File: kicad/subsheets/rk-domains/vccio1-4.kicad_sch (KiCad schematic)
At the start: 6 parts, among them U5 RK3566

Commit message: Mark as R1.0
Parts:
- renumbered C134 to C113, C129 to C114, C135 to C115, C137 to C116, R47 to R44
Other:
- company: (none) -> UVic Rocketry
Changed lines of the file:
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@@
 	(title_block
 		(title "VCCIO 1/2/3/4")
+		(date "2025-11-23")
+		(rev "1.0")
+		(company "UVic Rocketry")
+		(comment 1 "Author: Eric Handley")
 	)
 	(junction
@@
 		(on_board yes)
 		(dnp no)
-		(property "Reference" "R47"
+		(property "Reference" "R44"
 			(at 177.8 66.294 90)
 			(effects
@@
 			(project "srad-camera"
 				(path "/da62c771-e8c9-451f-8df1-ec995aadcb11/279fc251-45a8-41a3-8fcf-5855d7fe07da/746a399b-d324-4398-80ad-90e9781d2066"
-					(reference "R47")
+					(reference "R44")
 					(unit 1)
 				)
@@
 		(on_board yes)
 		(dnp no)
-		(property "Reference" "C129"
+		(property "Reference" "C114"
 			(at 179.832 75.9525 0)
 			(effects
@@
 			(project "srad-camera"
 				(path "/da62c771-e8c9-451f-8df1-ec995aadcb11/279fc251-45a8-41a3-8fcf-5855d7fe07da/746a399b-d324-4398-80ad-90e9781d2066"
-					(reference "C129")
+					(reference "C114")
 					(unit 1)
 				)
@@
 		(dnp no)
 		(fields_autoplaced yes)
-		(property "Reference" "#PWR077"
+		(property "Reference" "#PWR080"
 			(at 172.72 139.7 0)
 			(effects
@@
 			(project "srad-camera"
 				(path "/da62c771-e8c9-451f-8df1-ec995aadcb11/279fc251-45a8-41a3-8fcf-5855d7fe07da/746a399b-d324-4398-80ad-90e9781d2066"
-					(reference "#PWR077")
+					(reference "#PWR080")
 					(unit 1)
 				)
@@
 		(dnp no)
 		(fields_autoplaced yes)
-		(property "Reference" "#PWR069"
+		(property "Reference" "#PWR078"
 			(at 177.8 86.36 0)
 			(effects
@@
 			(project "srad-camera"
 				(path "/da62c771-e8c9-451f-8df1-ec995aadcb11/279fc251-45a8-41a3-8fcf-5855d7fe07da/746a399b-d324-4398-80ad-90e9781d2066"
-					(reference "#PWR069")
+					(reference "#PWR078")
 					(unit 1)
 				)
@@
 		(dnp no)
 		(fields_autoplaced yes)
-		(property "Reference" "#PWR074"
+		(property "Reference" "#PWR077"
 			(at 186.69 52.07 0)
 			(effects
@@
 			(project "srad-camera"
 				(path "/da62c771-e8c9-451f-8df1-ec995aadcb11/279fc251-45a8-41a3-8fcf-5855d7fe07da/746a399b-d324-4398-80ad-90e9781d2066"
-					(reference "#PWR074")
+					(reference "#PWR077")
 					(unit 1)
 				)
@@
 		(dnp no)
 		(fields_autoplaced yes)
-		(property "Reference" "C135"
+		(property "Reference" "C115"
 			(at 118.1164 88.2734 90)
 			(effects
@@
 			(project "srad-camera"
 				(path "/da62c771-e8c9-451f-8df1-ec995aadcb11/279fc251-45a8-41a3-8fcf-5855d7fe07da/746a399b-d324-4398-80ad-90e9781d2066"
-					(reference "C135")
+					(reference "C115")
 					(unit 1)
 				)
@@
 		(dnp no)
 		(fields_autoplaced yes)
-		(property "Reference" "C134"
+		(property "Reference" "C113"
 			(at 176.5236 46.3634 90)
 			(effects
@@
 			(project "srad-camera"
 				(path "/da62c771-e8c9-451f-8df1-ec995aadcb11/279fc251-45a8-41a3-8fcf-5855d7fe07da/746a399b-d324-4398-80ad-90e9781d2066"
-					(reference "C134")
+					(reference "C113")
 					(unit 1)
 				)
@@
 		(on_board yes)
 		(dnp no)
-		(property "Reference" "C137"
+		(property "Reference" "C116"
 			(at 174.752 129.2925 0)
 			(effects
@@
 			(project "srad-camera"
 				(path "/da62c771-e8c9-451f-8df1-ec995aadcb11/279fc251-45a8-41a3-8fcf-5855d7fe07da/746a399b-d324-4398-80ad-90e9781d2066"
-					(reference "C137")
+					(reference "C116")
 					(unit 1)
 				)
@@
 		(dnp no)
 		(fields_autoplaced yes)
-		(property "Reference" "#PWR075"
+		(property "Reference" "#PWR079"
 			(at 107.95 93.98 0)
 			(effects
@@
 			(project "srad-camera"
 				(path "/da62c771-e8c9-451f-8df1-ec995aadcb11/279fc251-45a8-41a3-8fcf-5855d7fe07da/746a399b-d324-4398-80ad-90e9781d2066"
-					(reference "#PWR075")
+					(reference "#PWR079")
 					(unit 1)
 				)

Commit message: Annotations
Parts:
- renumbered C113 to C126, C114 to C127, C115 to C128, C116 to C129, R44 to R47
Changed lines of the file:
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@@
 		(on_board yes)
 		(dnp no)
-		(property "Reference" "R44"
+		(property "Reference" "R47"
 			(at 177.8 66.294 90)
 			(effects
@@
 			(project "srad-camera"
 				(path "/da62c771-e8c9-451f-8df1-ec995aadcb11/279fc251-45a8-41a3-8fcf-5855d7fe07da/746a399b-d324-4398-80ad-90e9781d2066"
-					(reference "R44")
+					(reference "R47")
 					(unit 1)
 				)
@@
 		(on_board yes)
 		(dnp no)
-		(property "Reference" "C114"
+		(property "Reference" "C127"
 			(at 179.832 75.9525 0)
 			(effects
@@
 			(project "srad-camera"
 				(path "/da62c771-e8c9-451f-8df1-ec995aadcb11/279fc251-45a8-41a3-8fcf-5855d7fe07da/746a399b-d324-4398-80ad-90e9781d2066"
-					(reference "C114")
+					(reference "C127")
 					(unit 1)
 				)
@@
 		(dnp no)
 		(fields_autoplaced yes)
-		(property "Reference" "#PWR080"
+		(property "Reference" "#PWR090"
 			(at 172.72 139.7 0)
 			(effects
@@
 			(project "srad-camera"
 				(path "/da62c771-e8c9-451f-8df1-ec995aadcb11/279fc251-45a8-41a3-8fcf-5855d7fe07da/746a399b-d324-4398-80ad-90e9781d2066"
-					(reference "#PWR080")
+					(reference "#PWR090")
 					(unit 1)
 				)
@@
 		(dnp no)
 		(fields_autoplaced yes)
-		(property "Reference" "#PWR078"
+		(property "Reference" "#PWR088"
 			(at 177.8 86.36 0)
 			(effects
@@
 			(project "srad-camera"
 				(path "/da62c771-e8c9-451f-8df1-ec995aadcb11/279fc251-45a8-41a3-8fcf-5855d7fe07da/746a399b-d324-4398-80ad-90e9781d2066"
-					(reference "#PWR078")
+					(reference "#PWR088")
 					(unit 1)
 				)
@@
 		(dnp no)
 		(fields_autoplaced yes)
-		(property "Reference" "#PWR077"
+		(property "Reference" "#PWR087"
 			(at 186.69 52.07 0)
 			(effects
@@
 			(project "srad-camera"
 				(path "/da62c771-e8c9-451f-8df1-ec995aadcb11/279fc251-45a8-41a3-8fcf-5855d7fe07da/746a399b-d324-4398-80ad-90e9781d2066"
-					(reference "#PWR077")
+					(reference "#PWR087")
 					(unit 1)
 				)
@@
 		(dnp no)
 		(fields_autoplaced yes)
-		(property "Reference" "C115"
+		(property "Reference" "C128"
 			(at 118.1164 88.2734 90)
 			(effects
@@
 			(project "srad-camera"
 				(path "/da62c771-e8c9-451f-8df1-ec995aadcb11/279fc251-45a8-41a3-8fcf-5855d7fe07da/746a399b-d324-4398-80ad-90e9781d2066"
-					(reference "C115")
+					(reference "C128")
 					(unit 1)
 				)
@@
 		(dnp no)
 		(fields_autoplaced yes)
-		(property "Reference" "C113"
+		(property "Reference" "C126"
 			(at 176.5236 46.3634 90)
 			(effects
@@
 			(project "srad-camera"
 				(path "/da62c771-e8c9-451f-8df1-ec995aadcb11/279fc251-45a8-41a3-8fcf-5855d7fe07da/746a399b-d324-4398-80ad-90e9781d2066"
-					(reference "C113")
+					(reference "C126")
 					(unit 1)
 				)
@@
 		(on_board yes)
 		(dnp no)
-		(property "Reference" "C116"
+		(property "Reference" "C129"
 			(at 174.752 129.2925 0)
 			(effects
@@
 			(project "srad-camera"
 				(path "/da62c771-e8c9-451f-8df1-ec995aadcb11/279fc251-45a8-41a3-8fcf-5855d7fe07da/746a399b-d324-4398-80ad-90e9781d2066"
-					(reference "C116")
+					(reference "C129")
 					(unit 1)
 				)
@@
 		(dnp no)
 		(fields_autoplaced yes)
-		(property "Reference" "#PWR079"
+		(property "Reference" "#PWR089"
 			(at 107.95 93.98 0)
 			(effects
@@
 			(project "srad-camera"
 				(path "/da62c771-e8c9-451f-8df1-ec995aadcb11/279fc251-45a8-41a3-8fcf-5855d7fe07da/746a399b-d324-4398-80ad-90e9781d2066"
-					(reference "#PWR079")
+					(reference "#PWR089")
 					(unit 1)
 				)

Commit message: Start on PCB design
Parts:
- C124: renamed from C126; footprint (none) -> Capacitor_SMD:C_0402_1005Metric; LCSC PART NAME (none) -> C1525
- C125: renamed from C127; footprint (none) -> Capacitor_SMD:C_0402_1005Metric; LCSC PART NAME (none) -> C1525
- C126: renamed from C128; footprint (none) -> Capacitor_SMD:C_0402_1005Metric; LCSC PART NAME (none) -> C1525
- C127: renamed from C129; footprint (none) -> Capacitor_SMD:C_0402_1005Metric; LCSC PART NAME (none) -> C1525
- R48: renamed from R47; footprint (none) -> Resistor_SMD:R_0402_1005Metric; LCSC PART NAME (none) -> C25092
- U5: LCSC PART NAME RK3566 -> (none)
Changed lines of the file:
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@@
 		(on_board yes)
 		(dnp no)
-		(property "Reference" "R47"
+		(property "Reference" "R48"
 			(at 177.8 66.294 90)
 			(effects
@@
 			)
 		)
-		(property "Footprint" ""
+		(property "Footprint" "Resistor_SMD:R_0402_1005Metric"
 			(at 181.61 69.85 0)
 			(effects
@@
 		(property "SUPPLEMENTARY FEATURES" ""
 			(at 181.61 69.85 0)
+			(effects
+				(font
+					(size 1.27 1.27)
+				)
+				(hide yes)
+			)
+		)
+		(property "LCSC PART NAME" "C25092"
+			(at 181.61 69.85 90)
 			(effects
 				(font
@@
 			(project "srad-camera"
 				(path "/da62c771-e8c9-451f-8df1-ec995aadcb11/279fc251-45a8-41a3-8fcf-5855d7fe07da/746a399b-d324-4398-80ad-90e9781d2066"
-					(reference "R47")
+					(reference "R48")
 					(unit 1)
 				)
@@
 		(on_board yes)
 		(dnp no)
-		(property "Reference" "C127"
+		(property "Reference" "C125"
 			(at 179.832 75.9525 0)
 			(effects
@@
 			)
 		)
-		(property "Footprint" ""
+		(property "Footprint" "Capacitor_SMD:C_0402_1005Metric"
 			(at 177.8 76.2 0)
 			(effects
@@
 			)
 		)
-		(property "V" ""
-			(at 177.8 76.2 90)
+		(property "LCSC PART NAME" "C1525"
+			(at 177.8 76.2 0)
 			(effects
 				(font
@@
 			(project "srad-camera"
 				(path "/da62c771-e8c9-451f-8df1-ec995aadcb11/279fc251-45a8-41a3-8fcf-5855d7fe07da/746a399b-d324-4398-80ad-90e9781d2066"
-					(reference "C127")
+					(reference "C125")
 					(unit 1)
 				)
@@
 		(dnp no)
 		(fields_autoplaced yes)
-		(property "Reference" "#PWR090"
+		(property "Reference" "#PWR089"
 			(at 172.72 139.7 0)
 			(effects
@@
 			(project "srad-camera"
 				(path "/da62c771-e8c9-451f-8df1-ec995aadcb11/279fc251-45a8-41a3-8fcf-5855d7fe07da/746a399b-d324-4398-80ad-90e9781d2066"
-					(reference "#PWR090")
+					(reference "#PWR089")
 					(unit 1)
 				)
@@
 		(dnp no)
 		(fields_autoplaced yes)
-		(property "Reference" "#PWR088"
+		(property "Reference" "#PWR087"
 			(at 177.8 86.36 0)
 			(effects
@@
 			(project "srad-camera"
 				(path "/da62c771-e8c9-451f-8df1-ec995aadcb11/279fc251-45a8-41a3-8fcf-5855d7fe07da/746a399b-d324-4398-80ad-90e9781d2066"
-					(reference "#PWR088")
+					(reference "#PWR087")
 					(unit 1)
 				)
@@
 		(dnp no)
 		(fields_autoplaced yes)
-		(property "Reference" "#PWR087"
+		(property "Reference" "#PWR086"
 			(at 186.69 52.07 0)
 			(effects
@@
 			(project "srad-camera"
 				(path "/da62c771-e8c9-451f-8df1-ec995aadcb11/279fc251-45a8-41a3-8fcf-5855d7fe07da/746a399b-d324-4398-80ad-90e9781d2066"
-					(reference "#PWR087")
+					(reference "#PWR086")
 					(unit 1)
 				)
@@
 		(dnp no)
 		(fields_autoplaced yes)
-		(property "Reference" "C128"
+		(property "Reference" "C126"
 			(at 118.1164 88.2734 90)
 			(effects
@@
 			)
 		)
-		(property "Footprint" ""
+		(property "Footprint" "Capacitor_SMD:C_0402_1005Metric"
 			(at 118.11 93.98 0)
 			(effects
@@
 			)
 		)
-		(property "V" ""
+		(property "LCSC PART NAME" "C1525"
 			(at 118.11 93.98 90)
 			(effects
@@
 			(project "srad-camera"
 				(path "/da62c771-e8c9-451f-8df1-ec995aadcb11/279fc251-45a8-41a3-8fcf-5855d7fe07da/746a399b-d324-4398-80ad-90e9781d2066"
-					(reference "C128")
+					(reference "C126")
 					(unit 1)
 				)
@@
 		(dnp no)
 		(fields_autoplaced yes)
-		(property "Reference" "C126"
+		(property "Reference" "C124"
 			(at 176.5236 46.3634 90)
 			(effects
@@
 			)
 		)
-		(property "Footprint" ""
+		(property "Footprint" "Capacitor_SMD:C_0402_1005Metric"
 			(at 176.53 52.07 0)
 			(effects
@@
 			)
 		)
-		(property "V" ""
+		(property "LCSC PART NAME" "C1525"
 			(at 176.53 52.07 90)
 			(effects
@@
 			(project "srad-camera"
 				(path "/da62c771-e8c9-451f-8df1-ec995aadcb11/279fc251-45a8-41a3-8fcf-5855d7fe07da/746a399b-d324-4398-80ad-90e9781d2066"
-					(reference "C126")
+					(reference "C124")
 					(unit 1)
 				)
@@
 			)
 		)
-		(property "LCSC PART NAME" "RK3566"
+		(property "LCSC PART NAME" ""
 			(at 207.772 92.71 0)
 			(effects
@@
 		(on_board yes)
 		(dnp no)
-		(property "Reference" "C129"
+		(property "Reference" "C127"
 			(at 174.752 129.2925 0)
 			(effects
@@
 			)
 		)
-		(property "Footprint" ""
+		(property "Footprint" "Capacitor_SMD:C_0402_1005Metric"
 			(at 172.72 129.54 0)
 			(effects
@@
 			)
 		)
-		(property "V" ""
-			(at 172.72 129.54 90)
+		(property "LCSC PART NAME" "C1525"
+			(at 172.72 129.54 0)
 			(effects
 				(font
@@
 			(project "srad-camera"
 				(path "/da62c771-e8c9-451f-8df1-ec995aadcb11/279fc251-45a8-41a3-8fcf-5855d7fe07da/746a399b-d324-4398-80ad-90e9781d2066"
-					(reference "C129")
+					(reference "C127")
 					(unit 1)
 				)
@@
 		(dnp no)
 		(fields_autoplaced yes)
-		(property "Reference" "#PWR089"
+		(property "Reference" "#PWR088"
 			(at 107.95 93.98 0)
 			(effects
@@
 			(project "srad-camera"
 				(path "/da62c771-e8c9-451f-8df1-ec995aadcb11/279fc251-45a8-41a3-8fcf-5855d7fe07da/746a399b-d324-4398-80ad-90e9781d2066"
-					(reference "#PWR089")
+					(reference "#PWR088")
 					(unit 1)
 				)

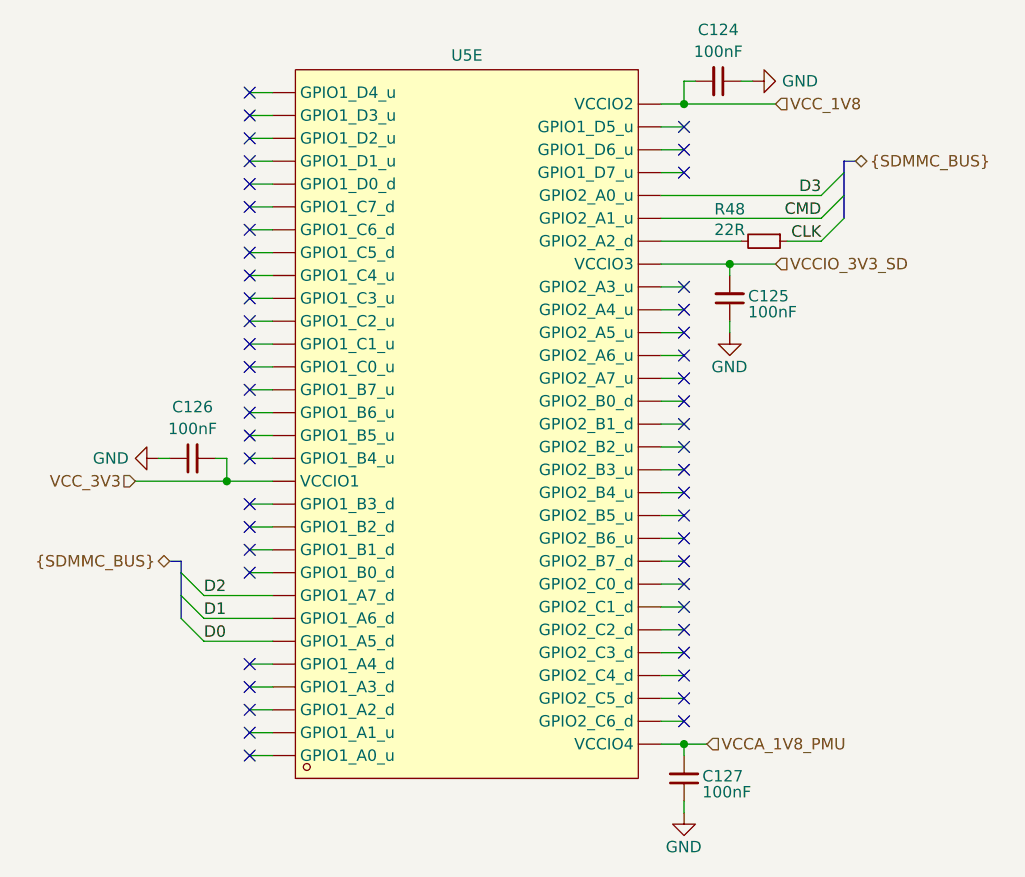
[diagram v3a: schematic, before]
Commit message: Remove power/decoupling for unused power domains
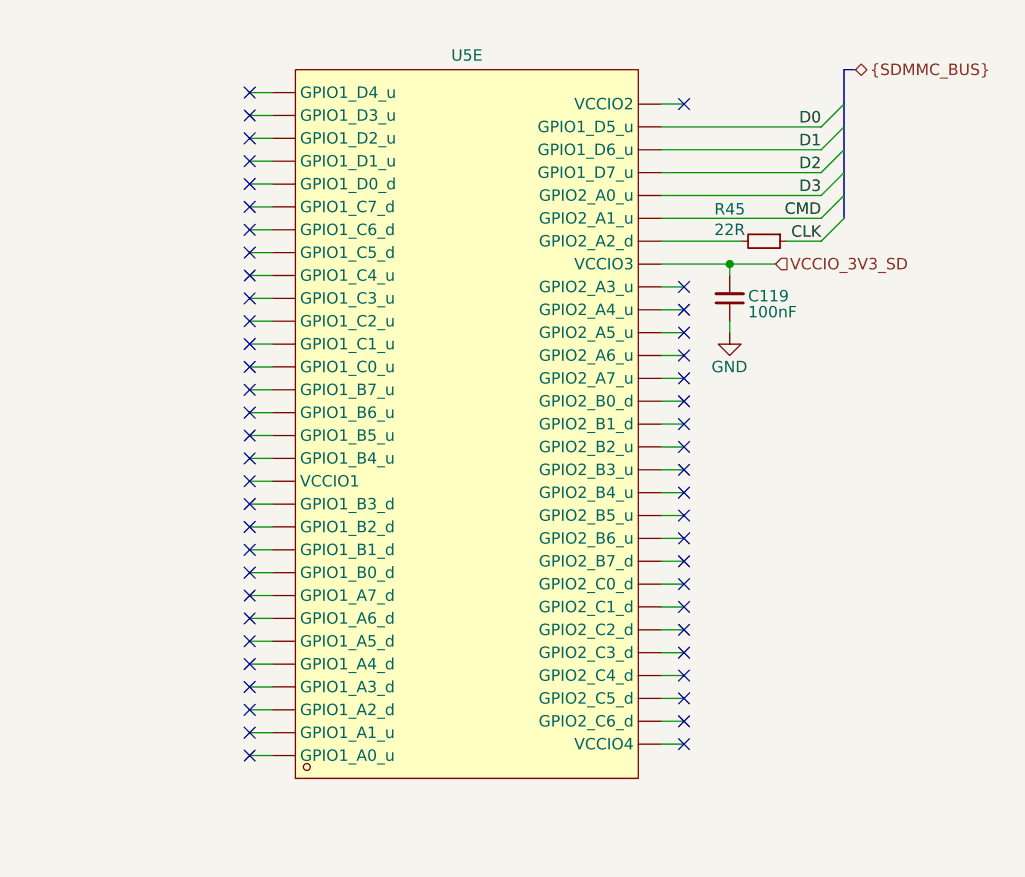
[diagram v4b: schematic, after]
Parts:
- removed C124, C126, C127: 100nF, Capacitor_SMD:C_0402_1005Metric, symbol Device:C_Small
- renumbered C125 to C119, R48 to R45
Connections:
- net D0: now also U5.1E20 (GPIO1_D5_u); no longer U5.B24 (GPIO1_A5_d)
- net D1: now also U5.1F19 (GPIO1_D6_u); no longer U5.1A14 (GPIO1_A6_d)
- net D2: now also U5.1D20 (GPIO1_D7_u); no longer U5.B25 (GPIO1_A7_d)
- net VCCA_1V8_PMU: no longer names the net of U5.1E16 (VCCIO4)
- net VCC_1V8: no longer names the net of U5.1C13 (VCCIO2)
- net VCC_3V3: no longer names the net of U5.1D13 (VCCIO1)
- no-connect marks 49 -> 52

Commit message: PCB done besides fixing screwups + length matching
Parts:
- removed R45: 22R, Resistor_SMD:R_0402_1005Metric, symbol Device:R_Small
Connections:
- net CLK: now also U5.G38 (GPIO2_A2_d)
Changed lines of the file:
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@@
 	(wire
 		(pts
-			(xy 170.18 69.85) (xy 179.07 69.85)
+			(xy 170.18 69.85) (xy 187.96 69.85)
 		)
 		(stroke
@@
 		(pts
 			(xy 172.72 107.95) (xy 170.18 107.95)
-		)
-		(stroke
-			(width 0)
-			(type default)
-		)
-	)
-	(wire
-		(pts
-			(xy 184.15 69.85) (xy 187.96 69.85)
 		)
 		(stroke
@@
 		)
 	)
-	(symbol
-		(lib_id "Device:R_Small")
-		(at 181.61 69.85 270)
-		(unit 1)
-		(exclude_from_sim no)
-		(in_bom yes)
-		(on_board yes)
-		(dnp no)
-		(property "Reference" "R45"
-			(at 177.8 66.294 90)
-			(effects
-				(font
-					(size 1.27 1.27)
-				)
-			)
-		)
-		(property "Value" "22R"
-			(at 177.8 68.58 90)
-			(effects
-				(font
-					(size 1.27 1.27)
-				)
-			)
-		)
-		(property "Footprint" "Resistor_SMD:R_0402_1005Metric"
-			(at 181.61 69.85 0)
-			(effects
-				(font
-					(size 1.27 1.27)
-				)
-				(hide yes)
-			)
-		)
-		(property "Datasheet" "~"
-			(at 181.61 69.85 0)
-			(effects
-				(font
-					(size 1.27 1.27)
-				)
-				(hide yes)
-			)
-		)
-		(property "Description" "Resistor, small symbol"
-			(at 181.61 69.85 0)
-			(effects
-				(font
-					(size 1.27 1.27)
-				)
-				(hide yes)
-			)
-		)
-		(property "ADDITIONAL CARD DETECTION PINS" ""
-			(at 181.61 69.85 0)
-			(effects
-				(font
-					(size 1.27 1.27)
-				)
-				(hide yes)
-			)
-		)
-		(property "CARD CONNECTION MODE" ""
-			(at 181.61 69.85 0)
-			(effects
-				(font
-					(size 1.27 1.27)
-				)
-				(hide yes)
-			)
-		)
-		(property "CARD TYPE" ""
-			(at 181.61 69.85 0)
-			(effects
-				(font
-					(size 1.27 1.27)
-				)
-				(hide yes)
-			)
-		)
-		(property "CONNECTOR TYPE" ""
-			(at 181.61 69.85 0)
-			(effects
-				(font
-					(size 1.27 1.27)
-				)
-				(hide yes)
-			)
-		)
-		(property "SUPPLEMENTARY FEATURES" ""
-			(at 181.61 69.85 0)
-			(effects
-				(font
-					(size 1.27 1.27)
-				)
-				(hide yes)
-			)
-		)
-		(property "LCSC PART NAME" "C25092"
-			(at 181.61 69.85 90)
-			(effects
-				(font
-					(size 1.27 1.27)
-				)
-				(hide yes)
-			)
-		)
-		(pin "2"
-		)
-		(pin "1"
-		)
-		(instances
-			(project "srad-camera"
-				(path "/da62c771-e8c9-451f-8df1-ec995aadcb11/279fc251-45a8-41a3-8fcf-5855d7fe07da/746a399b-d324-4398-80ad-90e9781d2066"
-					(reference "R45")
-					(unit 1)
-				)
-			)
-		)
-	)
